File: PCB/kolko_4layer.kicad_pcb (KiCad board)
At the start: 4 copper layers, 141.4 x 141.4 mm, 82 parts, among them IC1 74HC4067PW-Q100J, J1 USB_C_Receptacle_USB2.0_16P, J2 Conn_01x02_Socket, J3 Conn_01x04_Socket, SW1 RST, SW2 BOOT, U1 ESP32-S3-WROOM-1, U2 USBLC6-2SC6, U3 AMS1117-3.3

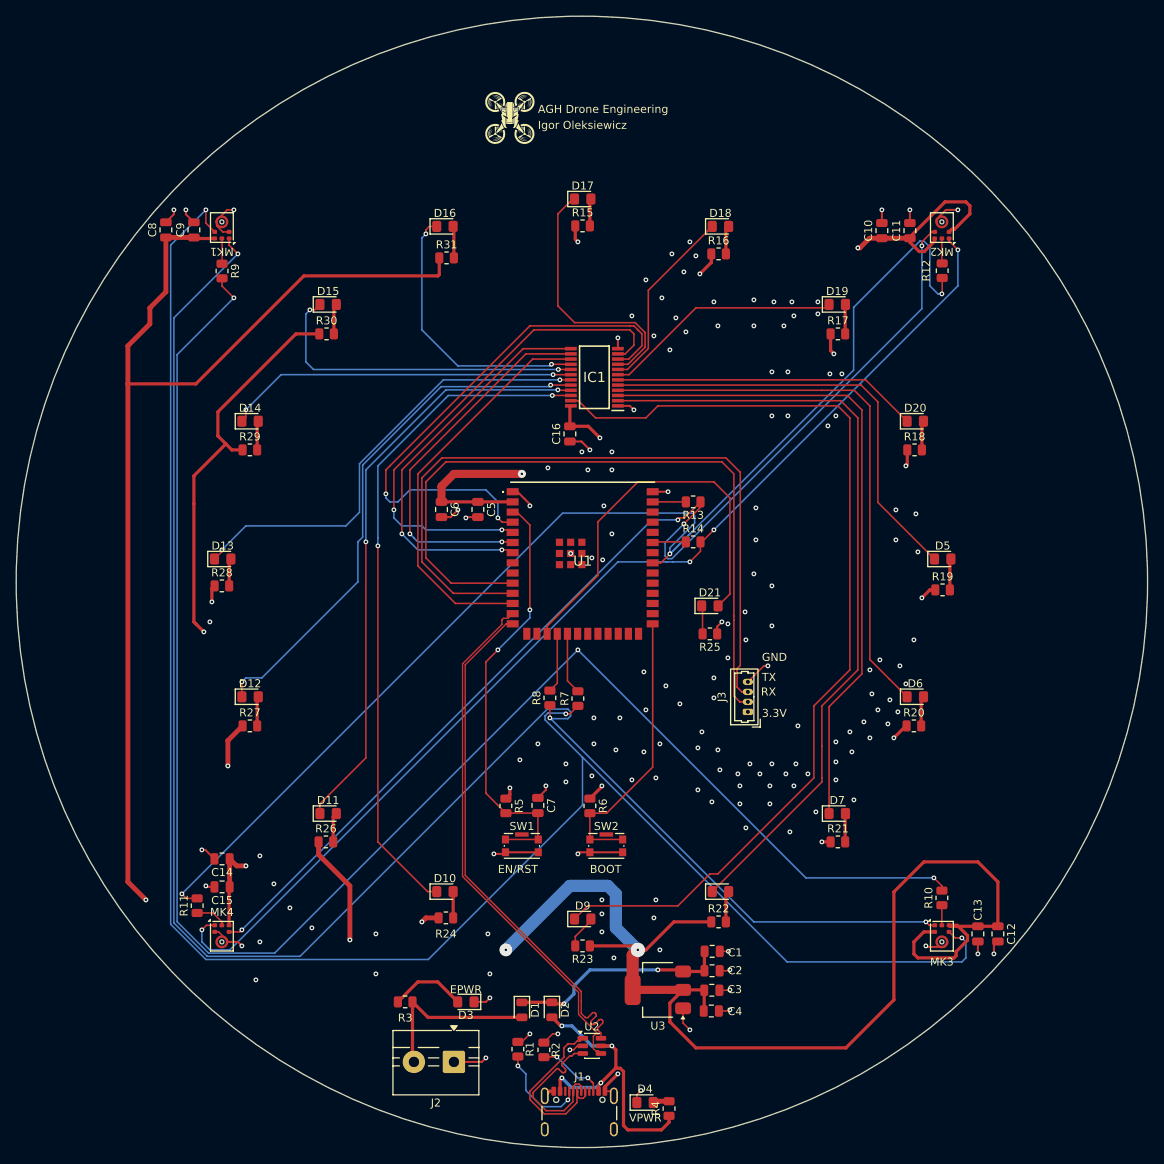
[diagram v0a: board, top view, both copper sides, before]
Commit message: equal length of microphones
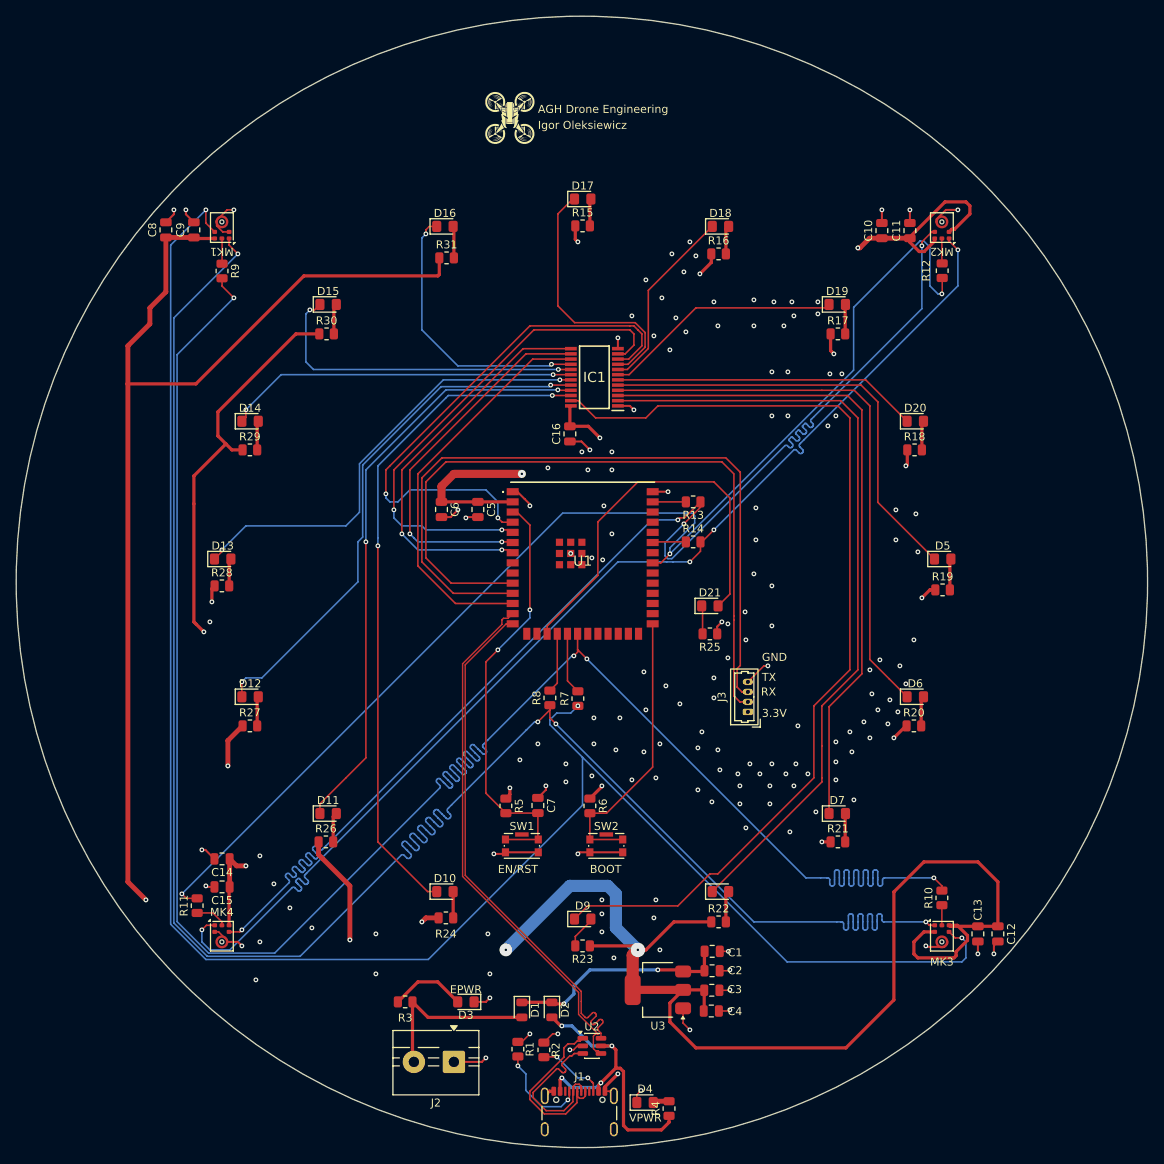
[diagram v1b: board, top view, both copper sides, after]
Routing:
- net /DATAA: track 209.7 -> 252.3 mm, vias 3 -> 4
- net /WSA: track 217.3 -> 244.7 mm, vias 3 -> 4
- net /BCLKB: track 145.4 -> 161.0 mm
- net /WSB: track 139.7 -> 145.0 mm
- net /DATAB: track 161.5 -> 157.1 mm
- net /BCLKA: track 236.8 -> 235.5 mm

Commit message: add vias
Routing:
- net GND: vias 165 -> 305

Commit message: better vias
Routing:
- net GND: vias 305 -> 359

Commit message: biger drone loogo
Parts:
- removed the REF** at (136.5, 40.5)
- added REF**: Drone_Logo_12mm_Silkscreen, muxy2:Drone_Logo_12mm_Silkscreen, F.Cu at (134.8, 40.5)

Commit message: add mounting holes
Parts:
- added M2: MountingHole_2.2mm_M2, MountingHole:MountingHole_2.2mm_M2, F.Cu at (145.5, 32.2)
- added M2: MountingHole_2.2mm_M2, MountingHole:MountingHole_2.2mm_M2, F.Cu at (80.5, 98.8)
- added M2: MountingHole_2.2mm_M2, MountingHole:MountingHole_2.2mm_M2, F.Cu at (210.5, 99.0)

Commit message: kosmetyczne zmiany
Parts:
- D1, D2: footprint LED_SMD:LED_0805_2012Metric -> Diode_SMD:D_SMB
- IC1: footprint muxy2:SOP65P640X110-24N -> Package_SO:TSSOP-24_4.4x7.8mm_P0.65mm
- moved D1 5.77 mm to (132.2, 151.5)
- moved D3 5.76 mm to (125.2, 150.8)
- moved R2 4.53 mm to (136.2, 157.5)
- moved R1 4.03 mm to (133.5, 157.4)
- moved J2 4.03 mm to (125.5, 158.0)
- moved R3 4.03 mm to (119.4, 150.5)
- moved D2 3.58 mm to (138.2, 151.2)
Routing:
- net VSUP: track 28.6 -> 35.3 mm
- net Net-(J1-CC2): track 8.73 -> 13.5 mm
- net GND: track 92.9 -> 88.6 mm, vias 359 -> 161
- net VBUS: track 39.5 -> 43.1 mm
- net Net-(J1-CC1): track 12.3 -> 15.7 mm
- net Net-(D3-A): track 9.55 -> 7.08 mm
- net /VEXT: track 22.1 -> 20.9 mm

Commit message: minor changes
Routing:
- net +3.3V: track 915.0 -> 912.8 mm
- net GND: vias 161 -> 358

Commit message: retorute usb
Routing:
- net /D_1-: track 20.8 -> 26.8 mm
- net /D_1+: track 23.0 -> 26.6 mm
- net /D_1MCU-: track 66.3 -> 68.0 mm
- net /D_1MCU+: track 66.2 -> 67.9 mm
- net GND: track 88.6 -> 87.7 mm, vias 358 -> 130
- added copper zone on In1.Cu, net +3.3V
